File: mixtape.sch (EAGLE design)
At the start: 53 parts, among them Q1 BSS123, SW1 WIREPADSMD1,27-254, SW2 WIREPADSMD1,27-254, U1 MCP73831, U5 ATMEGA32U4, U6 MIC5219-3.3, X1 MJ4435-R1503_03, X2 USB_MICROB_PLUGCONN-11752, Y2 8MHz

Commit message: Production Verions
Added repot to https://kitnic.it/ with 1-click BOM
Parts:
- removed F1: PTCSMD, SparkFun:PTCSMD
- removed JP10: FIDUCIALUFIDUCIAL, SparkFun:FIDUCIAL1X2
- removed JP3: (no value), SparkFun:M02-JST-2MM-SMT
- removed JP7: External Switch, SparkFun:M02PTH
- removed S2: Power Switch, SparkFun:SWITCH-SPSTSMD
- removed SW1, SW2: WIREPADSMD1,27-254, wirepad:WIREPADSMD1,27-254
- added BAT+, BAT-: (no value), wirepad:SMD5
- added C3, C6: 1uF, SparkFun-Capacitors:CAP0603-CAP
- added R1, R2: 33, SparkFun-Resistors:RESISTOR0603-RES
- added R4: 330, SparkFun-Resistors:RESISTOR0603-RES
- added SW: SWITCH_SMD, Gaudi:SWITCH_SMD
- added U$1, U$2: FIDUCIAL, adafruit:FIDUCIAL
- X1: value MJ4435-R1503_03 -> USB_B_SMD; device Gaudi:MJ4435-R1503_03 -> Gaudi:USB_B_SMD
- X2: value USB_MICROB_PLUGCONN-11752 -> PJ-327A; device SparkFun-Connectors:USB_MICROB_PLUGCONN-11752 -> Gaudi:PJ-327A
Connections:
- removed net N$13: Q1.D, SPEAKER.2
- removed net N$9: F1.2, JP7.2, S2.S
- new net N$2: C3.2, Q1.D, R1.1, R2.1
- new net N$3: C3.1, SPEAKER.1
- new net N$4: C6.2, R4.1, X2.3
- new net N$7: Q1.G, R3.2, X2.4
- net D10: now also R4.2
- net D9: no longer Q1.G, R3.2
- net GND: now also BAT-.P, C6.1, SPEAKER.2, X1.GND, X2.1, X2.5; no longer JP3.1, X1.1_1, X1.1_3, X1.1_4, X2.GND
- net MISO: now also SD.DATA_OUT; no longer SD.DATA_IN
- net MOSI: now also SD.DATA_IN; no longer SD.DATA_OUT
- net N$20: now also X1.D-; no longer X2.D-
- net N$21: now also X2.2; no longer X1.3_1, X1.3_3, X1.3_4
- net N$5: now also X1.D+; no longer X2.D+
- net RAW: now also R1.2, R2.2, SW.S1; no longer JP7.1, S2.P, SPEAKER.1
- net USB_VCC: now also X1.VCC; no longer X2.VCC
- net VBATT: now also BAT+.P, SW.COM; no longer F1.1, JP3.2
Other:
- moved on the sheet: SPEAKER

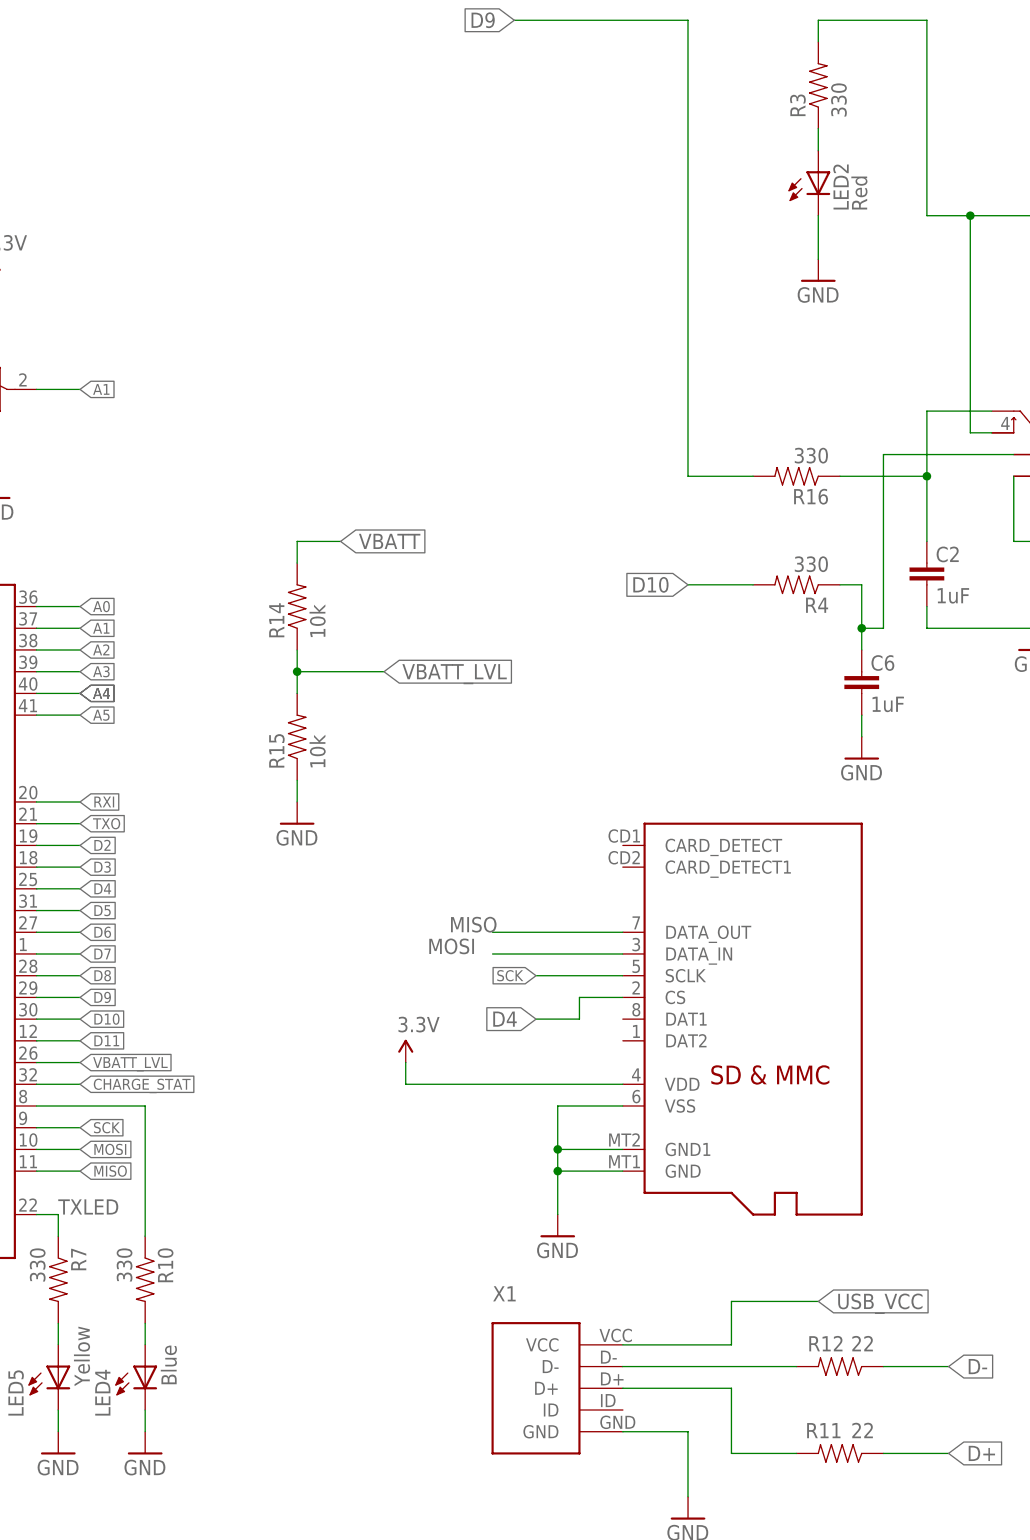
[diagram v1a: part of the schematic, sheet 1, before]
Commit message: corected error on USB port in BOM
plus minor updates
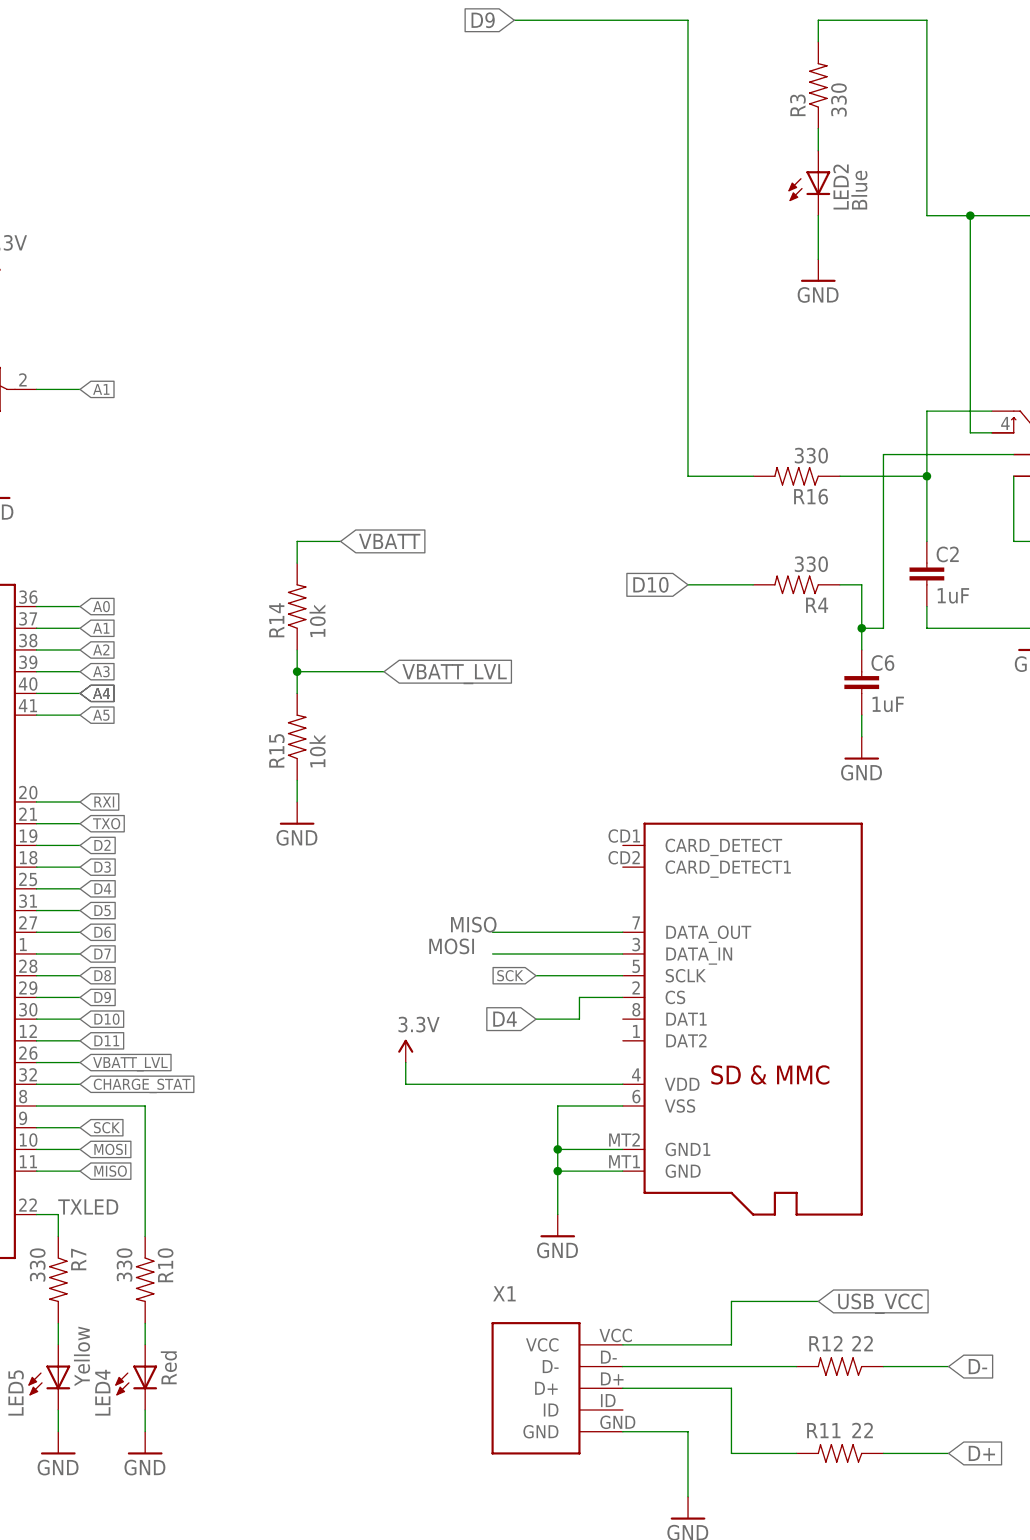
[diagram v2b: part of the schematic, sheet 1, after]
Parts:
- LED2: value Red -> Blue
- LED3: value Red -> Green
- LED4: value Blue -> Red
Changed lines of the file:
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@@
 <part name="GND1" library="SparkFun" deviceset="GND" device=""/>
 <part name="R3" library="SparkFun-Resistors" deviceset="RESISTOR" device="0603-RES" value="330"/>
-<part name="LED2" library="SparkFun" deviceset="LED" device="0603" value="Red"/>
+<part name="LED2" library="SparkFun" deviceset="LED" device="0603" value="Blue"/>
 <part name="GND11" library="supply1" deviceset="GND" device=""/>
 <part name="C9" library="SparkFun-Capacitors" deviceset="CAP" device="0603-CAP" value="4.7uF"/>
@@
 <part name="GND26" library="SparkFun" deviceset="GND" device=""/>
 <part name="R10" library="SparkFun-Resistors" deviceset="RESISTOR" device="0603-RES" value="330"/>
-<part name="LED4" library="SparkFun" deviceset="LED" device="0603" value="Blue"/>
+<part name="LED4" library="SparkFun" deviceset="LED" device="0603" value="Red"/>
 <part name="GND27" library="SparkFun" deviceset="GND" device=""/>
 <part name="R11" library="SparkFun-Resistors" deviceset="RESISTOR" device="0603-RES" value="22"/>
@@
 <part name="GND30" library="SparkFun" deviceset="GND" device=""/>
 <part name="R13" library="SparkFun-Resistors" deviceset="RESISTOR" device="0603-RES" value="330"/>
-<part name="LED3" library="SparkFun" deviceset="LED" device="0603" value="Red"/>
+<part name="LED3" library="SparkFun" deviceset="LED" device="0603" value="Green"/>
 <part name="GND31" library="SparkFun" deviceset="GND" device=""/>
 <part name="C14" library="SparkFun-Capacitors" deviceset="CAP" device="0603-CAP" value="0.1uF"/>
